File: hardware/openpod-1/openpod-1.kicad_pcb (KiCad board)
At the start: 4 copper layers, 53.3 x 90.2 mm, 78 parts, among them J1 USB_B_Micro, J2 AudioJack2_Ground, J3 Micro_SD_Card, Q1 TRANSISTOR_NPNSOT23-3, SW1 SW_Push, U1 MCP73831-2-OT, U2 SPX3819M5-L-3-3, U3 click-wheel, U4 ATSAMD21G18A-AUT, U5 AT42QT2120_COMMS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

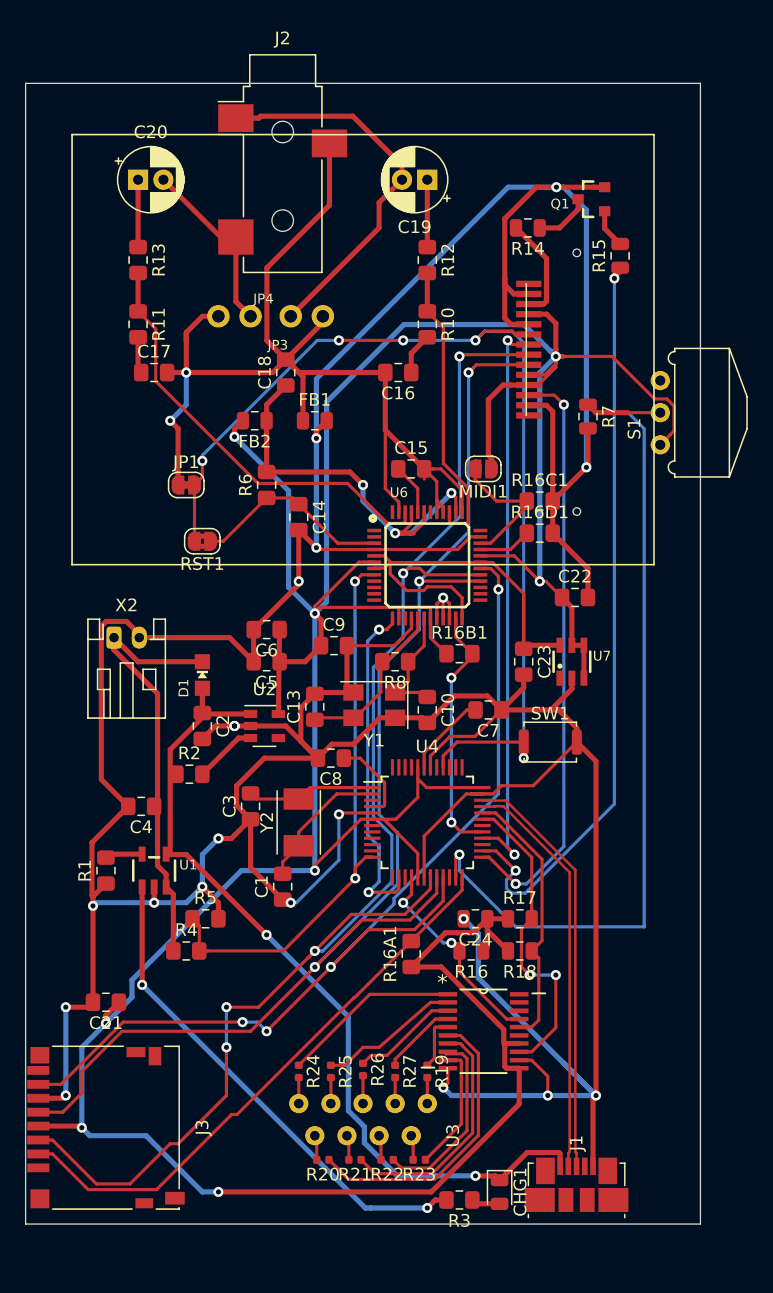
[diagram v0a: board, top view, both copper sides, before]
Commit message: update click wheel, use connectors
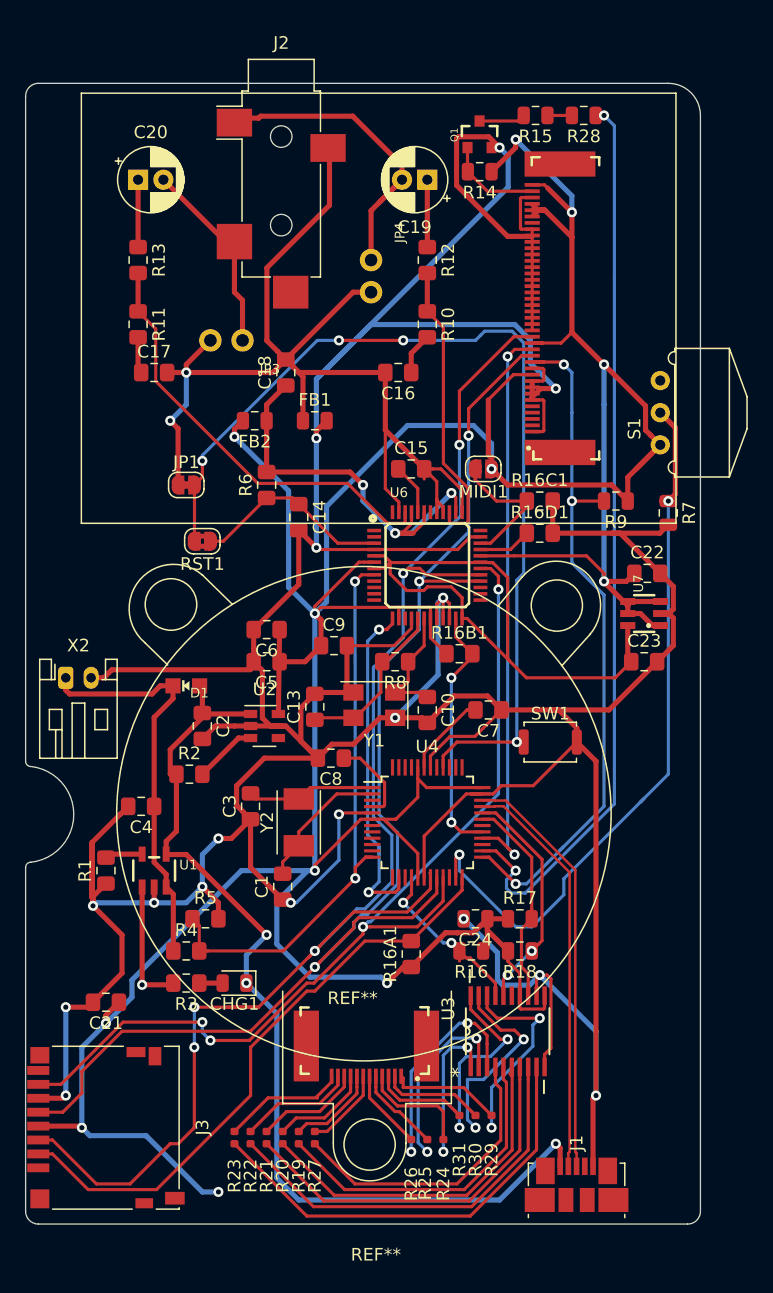
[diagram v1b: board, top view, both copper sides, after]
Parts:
- removed LCD1: JD-T1800, little-helper:JD-T1800
- added R28: 1, Resistor_SMD:R_0805_2012Metric, F.Cu at (120.3, 40.6)
- added R29: 1k, Resistor_SMD:R_0402_1005Metric, F.Cu at (113.0, 120.2)
- added R30: 1k, Resistor_SMD:R_0402_1005Metric, F.Cu at (111.8, 120.2)
- added R31: 1k, Resistor_SMD:R_0402_1005Metric, F.Cu at (110.5, 120.2)
- added R9: 10k, Resistor_SMD:R_0805_2012Metric, F.Cu at (122.9, 71.1)
- added U8: KWH018ST14-F01_4WSPI-TOP, sparkfun:FPC05040-17204, F.Cu at (116.8, 55.9)
- J2: footprint custom:Jack_3.5mm_CUI_SJ-3523-SMT_Horizontal-G -> Connector_Audio:Jack_3.5mm_CUI_SJ-3524-SMT_Horizontal
- Q1: value TRANSISTOR_NPNSOT23-3 -> 220mA/50V/3.5Ω; footprint little-helper:SOT23-3 -> sparkfun:SOT23-3
- R14: value 22 -> 10k
- R15: value 1k -> 1
- U7: value VREG_SOT23-6_DUALAP7312 -> TLV733P-Q1
- moved R3 27.6 mm to (88.9, 109.2)
- moved CHG1 26.7 mm to (92.7, 109.2), turned to 180 degrees
- moved R23 14.7 mm to (92.7, 121.4), turned to 90 degrees
- moved R15 13.0 mm to (116.5, 40.6), turned to 180 degrees
- moved R24 12.8 mm to (109.2, 122.1), turned to 90 degrees
- moved R19 11.4 mm to (97.8, 121.4), turned to 90 degrees
- moved R22 10.9 mm to (94.0, 121.4), turned to 90 degrees
- moved Q1 10.2 mm to (112.1, 42.2), turned to 0 degrees
- moved R7 9.92 mm to (127.0, 72.1)
- moved R25 9.62 mm to (108.0, 122.1), turned to 90 degrees
- moved C23 9.53 mm to (125.1, 83.8), turned to 0 degrees
- moved R27 8.23 mm to (99.1, 121.4), turned to 90 degrees
- moved R21 7.20 mm to (95.2, 121.4), turned to 90 degrees
- moved R26 7.12 mm to (106.7, 122.1), turned to 90 degrees
- moved U7 6.87 mm to (125.1, 80.0), turned to 90 degrees
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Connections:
- Q1 pad 1: Net-(Q1-Pad1) -> LEDK
- R14 pad 1: Net-(Q1-Pad3) -> +3V3
- R14 pad 2: Net-(LCD1-Pad3) -> LEDK
- R15 pad 1: D13 -> Net-(R15-Pad1)
- R15 pad 2: Net-(Q1-Pad1) -> Net-(Q1-Pad3)
- U3 pad 1: Net-(R24-Pad2) -> Net-(R29-Pad2)
- U3 pad 2: Net-(R25-Pad2) -> Net-(R30-Pad2)
- U3 pad 3: Net-(R26-Pad2) -> Net-(R31-Pad2)
- U3 pad 4: Net-(R27-Pad2) -> Net-(R24-Pad2)
- U3 pad 5: Net-(R19-Pad2) -> Net-(R25-Pad2)
- U3 pad 6: Net-(R20-Pad2) -> Net-(R26-Pad2)
- U3 pad 7: Net-(R21-Pad2) -> Net-(R27-Pad2)
- U3 pad 8: Net-(R22-Pad2) -> Net-(R19-Pad2)
- U3 pad 9: Net-(R23-Pad2) -> Net-(R20-Pad2)
- U5 pad 18: (no net) -> Net-(R29-Pad1)
- U5 pad 19: (no net) -> Net-(R30-Pad1)
- U5 pad 20: (no net) -> Net-(R31-Pad1)
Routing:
- net Net-(R3-Pad2): track 39.4 -> 9.70 mm, vias 2 -> 1
- net Net-(R23-Pad1): track 10.1 -> 35.0 mm
- net Net-(R19-Pad1): track 4.27 -> 25.8 mm
- net Earth: track 416.8 -> 438.0 mm, vias 20 -> 17
- net VBUS: track 66.3 -> 86.8 mm, vias 2 -> 3
- net +3V3: track 315.5 -> 334.4 mm, vias 8 -> 12
- net Net-(R27-Pad1): track 5.96 -> 23.4 mm
- net Net-(R22-Pad1): track 15.1 -> 32.4 mm
- net +1V8: track 31.1 -> 48.4 mm
- net Net-(R29-Pad1): track 0.00 -> 15.7 mm, vias 0 -> 2
- net Net-(R30-Pad1): track 0.00 -> 15.4 mm, vias 0 -> 2
- net Net-(R31-Pad1): track 0.00 -> 14.7 mm, vias 0 -> 2
- net D13: track 59.5 -> 72.0 mm
- net Net-(R21-Pad1): track 19.1 -> 30.1 mm
- net D11: track 46.6 -> 55.8 mm, vias 2 -> 3
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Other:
- outline, holes or cut-outs redrawn
- rule trace_min: 0.2 -> 0.24892

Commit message: revision 1
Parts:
- added H1: MountingHole, MountingHole:MountingHole_2.2mm_M2_DIN965_Pad, F.Cu at (87.9, 79.2)
- added H2: MountingHole, MountingHole:MountingHole_2.2mm_M2_DIN965_Pad, F.Cu at (117.9, 79.2)
- added H3: MountingHole, MountingHole:MountingHole_2.2mm_M2_DIN965_Pad, F.Cu at (103.6, 121.4)
- added HS1: Heatsink_Pad, custom:medium-thermal, B.Cu at (87.0, 102.9)
- added HS2: Heatsink_Pad, custom:medium-thermal, B.Cu at (85.9, 106.7)
- added HS3: Heatsink_Pad, custom:thermal, B.Cu at (109.2, 101.0)
- added HS4: Heatsink_Pad, custom:small-thermal, B.Cu at (126.5, 82.3)
- C19, C20: footprint Capacitor_THT:CP_Radial_D5.0mm_P2.00mm -> Capacitor_SMD:CP_Elec_6.3x5.4
- J2: value AudioJack2_Ground -> SJ-3524-SMT-jack
- SW1: footprint Button_Switch_SMD:SW_Push_SPST_NO_Alps_SKRK -> reset-button:PTS647
- X2: footprint Connector_JST:JST_PH_S2B-PH-K_1x02_P2.00mm_Horizontal -> little-helper:JST-2-SMD
- moved SW1 13.6 mm to (122.6, 102.9), turned to 90 degrees
- moved R1 8.89 mm to (82.8, 91.4), turned to 0 degrees
- moved C4 6.35 mm to (85.3, 88.9)
- moved C23 6.10 mm to (125.1, 89.9)
- moved JP3 5.99 mm to (88.9, 53.3), turned to 270 degrees
- moved R12 4.45 mm to (111.8, 54.4), turned to 180 degrees
- moved C19 4.19 mm to (106.9, 49.8)
- moved J1 3.81 mm to (123.6, 125.2)
- moved JP4 3.02 mm to (100.6, 54.1)
- moved X2 2.55 mm to (80.8, 83.0), turned to 180 degrees
- moved C22 2.01 mm to (126.0, 74.9)
- moved RST1 1.91 mm to (90.2, 72.4)
- moved R5 0.90 mm to (91.0, 104.8)
- moved J2 0.68 mm to (95.8, 45.1)
- moved U3 0.63 mm to (110.5, 118.7)
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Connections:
- J2 pad R: (no net) -> R_OUT
- J2 pad S: R_OUT -> AGND
- U4 pad 11: (no net) -> D8
- U6 pad 8: D9 -> D8
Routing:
- net Earth: track 438.0 -> 477.3 mm, vias 17 -> 40
- net +3V3: track 334.4 -> 364.5 mm, vias 12 -> 13
- net RESET: track 76.4 -> 105.5 mm, vias 4 -> 7
- net D8: track 0.00 -> 25.6 mm, vias 0 -> 2
- net D9: track 45.8 -> 25.2 mm, vias 2 -> 0
- net R_OUT: track 26.2 -> 13.1 mm
- net Net-(R1-Pad2): track 2.97 -> 8.88 mm
- net MISO: track 75.8 -> 81.0 mm
- net L_OUT: track 15.7 -> 11.5 mm
- net D-: track 32.4 -> 36.2 mm
- net D+: track 33.1 -> 36.9 mm
- net D2: track 57.7 -> 54.2 mm
- net VBUS: track 86.8 -> 83.6 mm, vias 3 -> 10
- net VBAT: track 32.0 -> 35.2 mm
- net D12: track 44.8 -> 46.8 mm
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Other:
- board text added: "Number of Layers: 2 PCB Thickness: 1.6mm Outer copper weight: 1oz Silkscreen color: white Soldermask color: black"
- board text added: "openpod rev-1.0"
